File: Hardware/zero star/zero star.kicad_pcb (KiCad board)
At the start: 4 copper layers, 38 x 38 mm, 142 parts, among them J1 USB_C_Receptacle_USB2.0_16P, J10 Conn_01x01, J11 Conn_01x01, J12 Conn_01x01, J13 Conn_01x01, J14 Conn_01x01, J15 Conn_01x01, J16 Conn_01x01, J17 Conn_01x01, J18 Conn_01x01, J19 Conn_01x01, J2 Conn_01x01, J20 Conn_01x01, J21 Conn_01x01, J22 ELRS, J23 GPS, J24 Conn_01x01, J25 Conn_01x01, J26 Conn_01x01, J27 Conn_01x01, J28 Conn_01x01, J29 Conn_01x01, J299 Conn_01x01, J3 上位机, J30 Conn_01x01, J31 Conn_01x01, J32 Conn_01x01, J33 Conn_01x01, J4 4-in-1 ESC, J5 光流, J6 VTX, J7 Conn_01x01, J8 Conn_01x01, J9 Conn_01x01, Q1 SS8050, SW1 SW_SPST, U1 STM32F405RGTx, U10 RT9193-33, U2 SY8303AIC, U3 SY8303AIC, U4 RT9193-33, U5 SPL06-001, U6 MPU-6050, U7 QMC5883L, U8 W25Q128JVE, U9 AT7456E, Y1 8Mhz, Y2 27Mhz

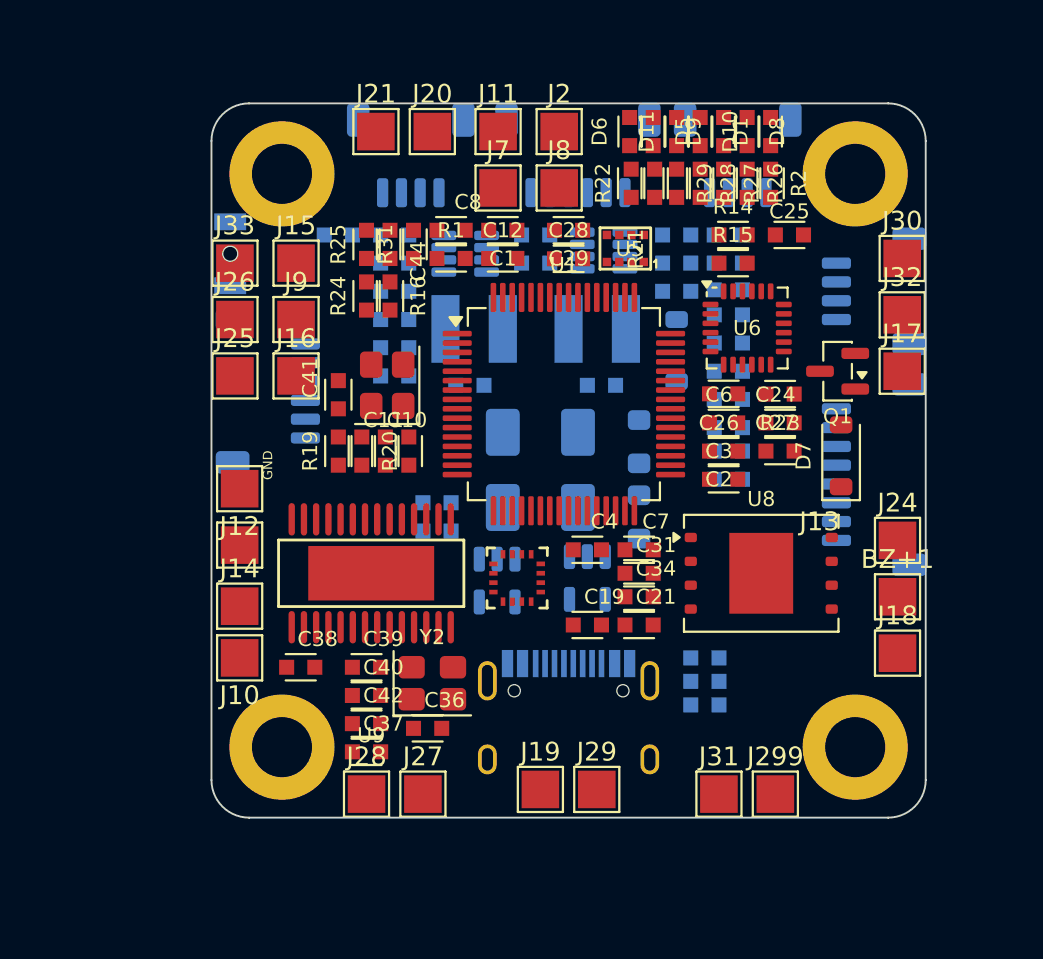
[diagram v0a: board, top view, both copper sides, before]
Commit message: HW v2.5.7: SPI CS pin swap, PCB layout v1, CubeMX update
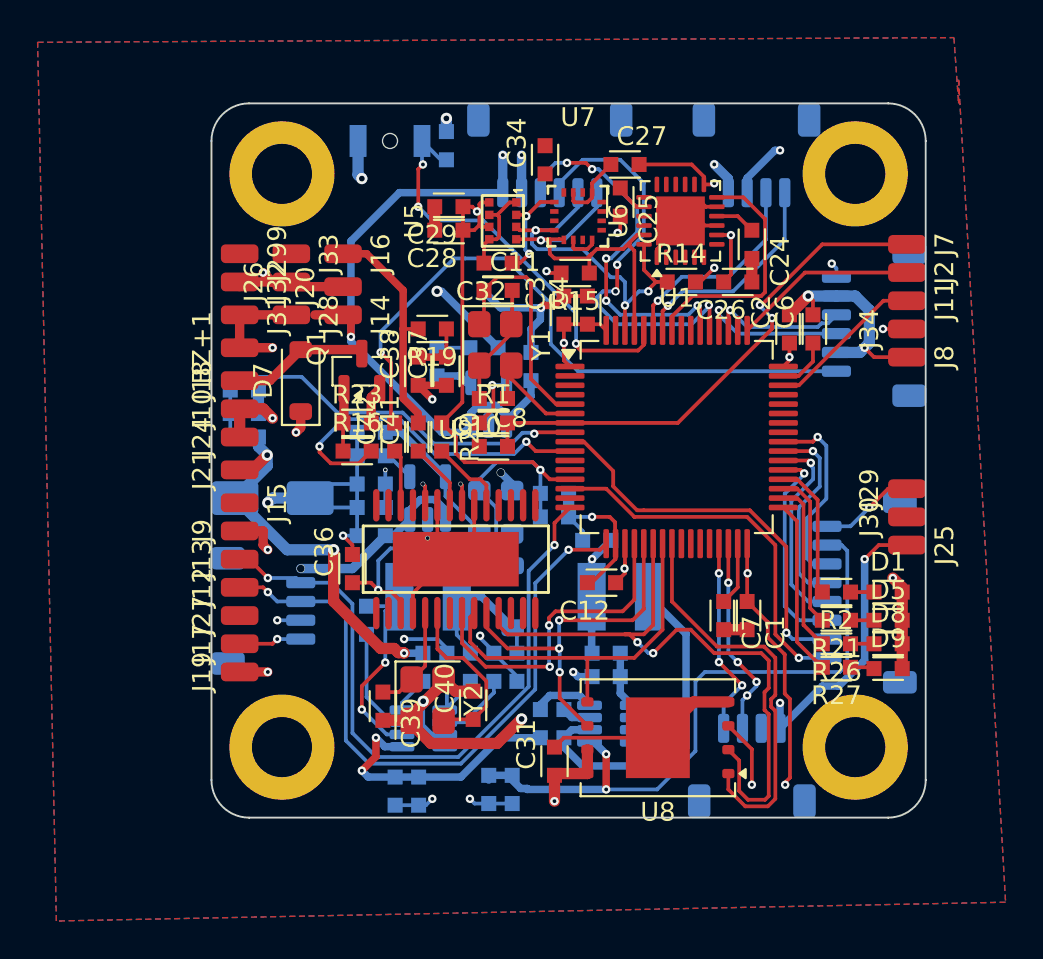
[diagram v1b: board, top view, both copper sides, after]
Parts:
- removed D10, D11, D6: LED_0603, PCM_fab:LED_0603
- removed D3: SS14, Diode_SMD:D_SMA
- removed J1: USB_C_Receptacle_USB2.0_16P, Connector_USB:USB_C_Receptacle_HRO_TYPE-C-31-M-12
- removed R12, R13: 5.1kΩ, PCM_fab:R_0603
- removed R22, R28, R29: 1kΩ, PCM_fab:R_0603
- removed R30: 10KΩ, PCM_fab:R_0603
- removed R31: 100KΩ, PCM_fab:R_0603
- added J34: Conn_01x01, Connector_Wire:SolderWirePad_1x01_SMD_1x2mm, F.Cu at (210.0, 80.0)
- BZ+1, J10, J11, J12, J13, J14, J15, J16, J17, J18, J19, J2, J20, J21, J24, J25, J26, J27, J28, J29, J299, J30, J31, J32, J33, J7, J8, J9: footprint TestPoint:TestPoint_Pad_2.0x2.0mm -> Connector_Wire:SolderWirePad_1x01_SMD_1x2mm
- C19, C21, C44, R24, R25: moved to B.Cu
- C32: moved to F.Cu
- J23: value GPS -> 光流
- J5: value 光流 -> GPS
- U6: footprint Sensor_Motion:InvenSense_QFN-24_4x4mm_P0.5mm -> Package_DFN_QFN:QFN-24-1EP_4x4mm_P0.5mm_EP2.6x2.6mm
- moved J299 40.5 mm to (174.5, 76.0), turned to -90 degrees
- moved J17 38.1 mm to (174.5, 96.8), turned to 90 degrees
- moved J18 37.9 mm to (174.5, 82.8), turned to 90 degrees
- moved BZ+1 37.4 mm to (174.5, 81.0), turned to 90 degrees
- moved J22 37.2 mm to (201.8, 103.2), turned to 180 degrees
- moved J25 36.9 mm to (210.0, 91.5), turned to -90 degrees
- moved J31 36.1 mm to (174.5, 79.2), turned to -90 degrees
- moved J24 35.4 mm to (174.5, 85.8), turned to 90 degrees
- moved J32 35.3 mm to (174.5, 77.5), turned to -90 degrees
- moved J5 35.0 mm to (175.8, 95.0), turned to 90 degrees
- moved C9 33.9 mm to (184.0, 104.6), turned to -90 degrees
- moved C13 33.2 mm to (182.8, 104.6), turned to -90 degrees
- moved D9 29.9 mm to (209.0, 98.1), turned to 0 degrees
- moved R9 29.9 mm to (197.0, 101.2), turned to 90 degrees
- moved D7 29.0 mm to (177.8, 82.8)
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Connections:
- C28 pad 1: +3.3V -> +3.3VA
- C29 pad 1: +3.3V -> +3.3VA
- C33 pad 2: Net-(C33-Pad2) -> GND
- C35 pad 2: Net-(C33-Pad2) -> GND
- C47 pad 2: Net-(C47-Pad2) -> GND
- C48 pad 2: Net-(C47-Pad2) -> GND
- J18 pad 1: /BZ- -> BZ-
- J23 pad 3: /UART2_TX -> /USART5_RX
- J23 pad 4: /UART2_RX -> /USART5_TX
- J23 pad 5: I2C1_SCL -> I2C1_SDA
- J23 pad 6: I2C1_SDA -> I2C1_SCL
- J3 pad 3: /USART1_TX -> /USART1_RX
- J3 pad 4: /USART1_RX -> /USART1_TX
- J4 pad 3: /M1 -> /M4
- J4 pad 4: /M2 -> /M3
- J4 pad 5: /M3 -> /M2
- J4 pad 6: /M4 -> /M1
- J5 pad 3: /USART5_TX -> /UART2_RX
- J5 pad 4: /USART5_RX -> /UART2_TX
- J6 pad 4: unconnected-(J6-Pin_4-Pad4) -> /USART4_RX
- R2 pad 2: LED_MODE -> LED_VTX
- R21 pad 2: LED_SYS -> LED_GPS
- R24 pad 2: /peripheral.kicad_sch/VBAT -> VBAT
- R26 pad 2: LED_LOG -> LED_MODE
- R27 pad 2: LED_VTX -> LED_SYS
- U1 pad 11: LED_SYS -> unconnected-(U1-PC3-Pad11)
- U1 pad 20: FLASH_CS -> OSD_CS
- U1 pad 24: LED_ERR -> FLASH_CS
- U1 pad 25: /CURR -> USB_DETECT
- U1 pad 27: LED_GPS -> unconnected-(U1-PB1-Pad27)
- U1 pad 28: LED_RX -> unconnected-(U1-PB2-Pad28)
- U1 pad 33: OSD_CS -> LED_SYS
- U1 pad 35: LED_LOG -> LED_GPS
- U1 pad 42: /USART1_TX -> unconnected-(U1-PA9-Pad42)
- U1 pad 43: /USART1_RX -> unconnected-(U1-PA10-Pad43)
- U1 pad 44: /USB_DM -> /USB_N
- U1 pad 45: /USB_DP -> /USB_P
- U1 pad 58: I2C1_SCL -> /USART1_TX
- U1 pad 59: I2C1_SDA -> /USART1_RX
- U1 pad 61: unconnected-(U1-PB8-Pad61) -> I2C1_SCL
- U1 pad 62: USB_DETECT -> I2C1_SDA
- U1 pad 9: unconnected-(U1-PC1-Pad9) -> /CURR
- U5 pad 2: +3.3V -> +3.3VA
- U5 pad 6: +3.3V -> +3.3VA
- U5 pad 8: +3.3V -> +3.3VA
- U6 pad 18: GND -> (no net)
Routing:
- net GND: track 0.00 -> 149.7 mm, vias 0 -> 23
- net +5V: track 0.00 -> 77.0 mm, vias 0 -> 10
- net VBAT: track 0.00 -> 70.0 mm, vias 0 -> 7
- net +3.3VA: track 0.00 -> 64.2 mm, vias 0 -> 9
- net +3.3V: track 0.00 -> 48.9 mm, vias 0 -> 12
- net /UART2_TX: track 0.00 -> 35.8 mm, vias 0 -> 2
- net /UART2_RX: track 0.00 -> 35.5 mm, vias 0 -> 2
- net VIDEO_OUT: track 0.00 -> 34.8 mm, vias 0 -> 1
- net SPI1_MISO: track 0.00 -> 34.5 mm, vias 0 -> 2
- net /NRST: track 0.00 -> 28.1 mm, vias 0 -> 2
- net VBAT_SENSE: track 0.00 -> 22.9 mm, vias 0 -> 1
- net /BOOT0: track 0.00 -> 22.6 mm, vias 0 -> 3
- net /USART5_TX: track 0.00 -> 22.3 mm, vias 0 -> 3
- net FLASH_CS: track 0.00 -> 21.4 mm
- net /CURR: track 0.00 -> 21.2 mm, vias 0 -> 1
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- added copper zone on In2.Cu, net +3.3VA
- added copper zone on In2.Cu, net +5V
- added copper zone on In2.Cu, net +5VA
- added copper zone on In2.Cu, net +9V
- added copper zone on B.Cu, net GND
- added copper zone on F.Cu, net GND
- added copper zone on In1.Cu, net GND
- removed copper zone on In1.Cu, net USB_DETECT
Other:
- board text removed: "GND"
